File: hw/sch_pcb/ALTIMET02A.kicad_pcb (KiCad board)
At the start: 2 copper layers, 40.1 x 19.8 mm, 14 parts, among them IC1 MS561101BA03-50, J2 HEADER_2x03, J3 HEADER_2x05_PARALLEL

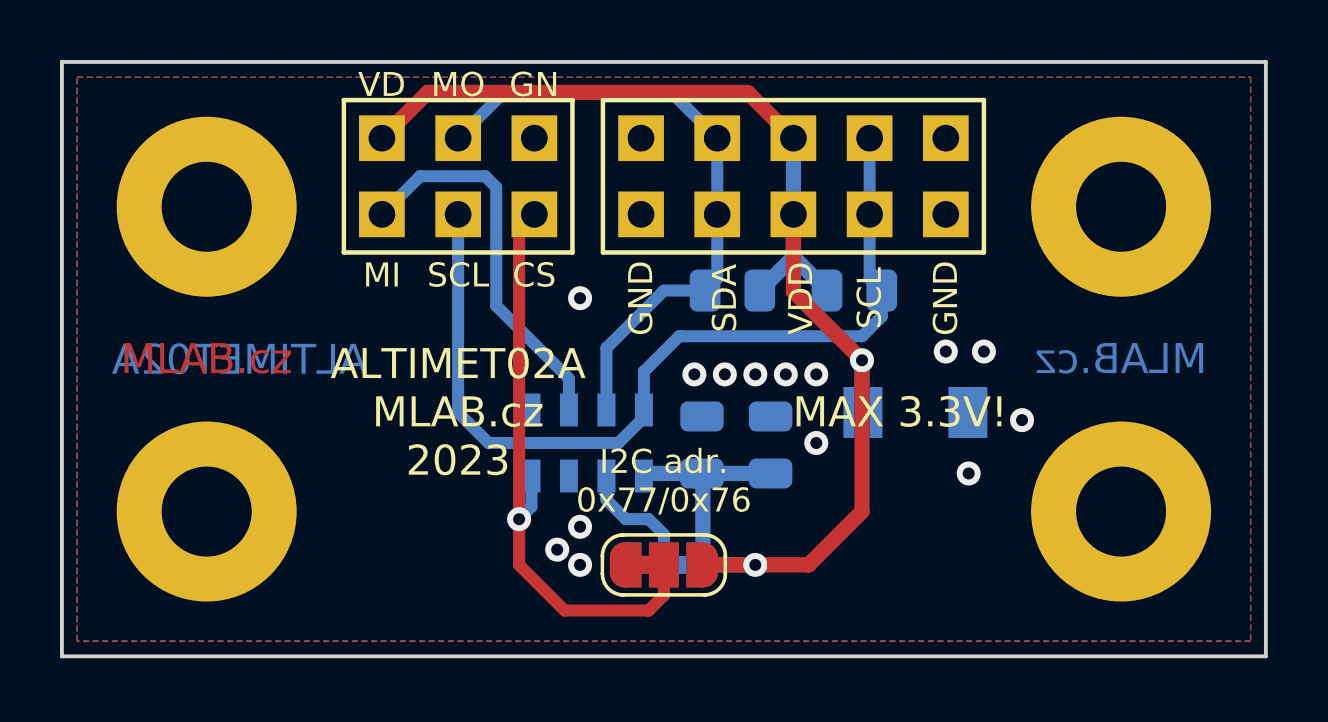
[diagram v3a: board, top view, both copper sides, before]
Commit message: Update submodule Fix CLK in silkscreen.
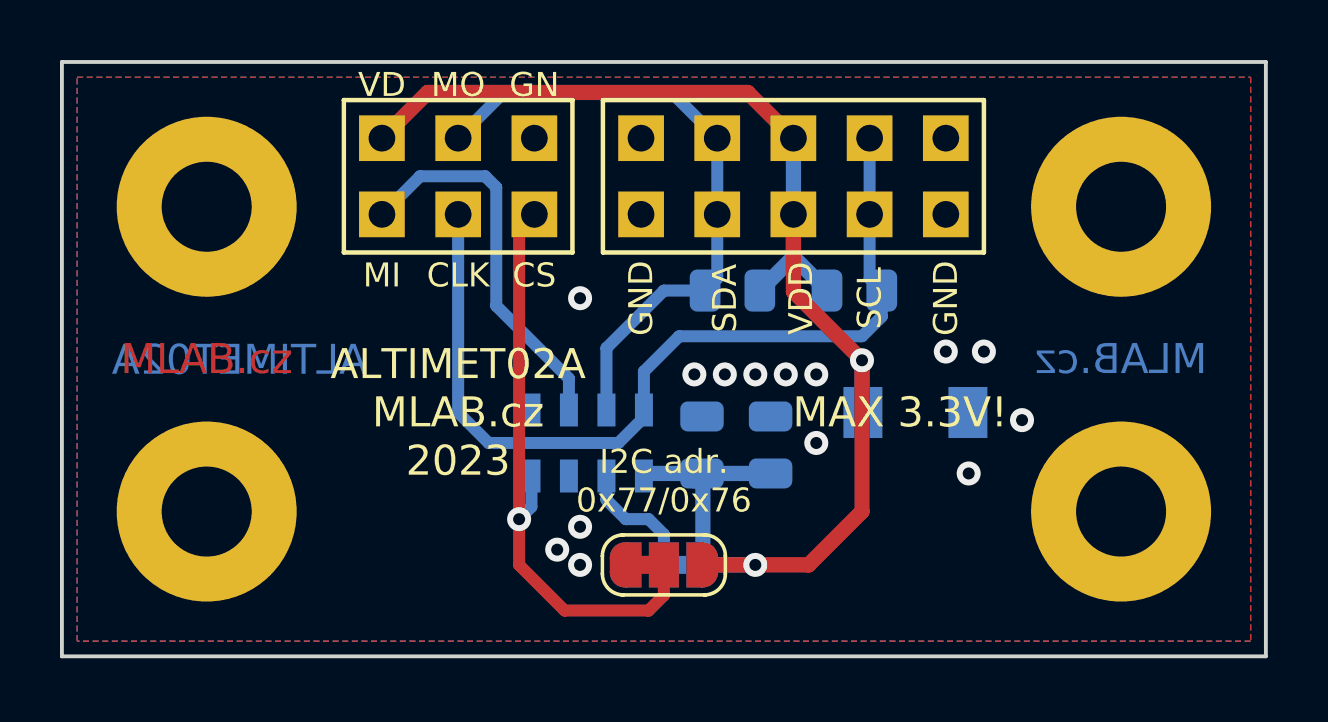
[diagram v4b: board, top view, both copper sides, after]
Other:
- board text added: "CLK"
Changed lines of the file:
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@@
     (effects (font (size 0.8 0.8) (thickness 0.15)))
   )
-  (gr_text "SCL" (at 125.222 103.886) (layer "F.SilkS")
+  (gr_text "CLK" (at 125.222 103.886) (layer "F.SilkS")
     (effects (font (size 0.8 0.8) (thickness 0.15)))
   )
@@
     (pts (xy 152.146 116.586) (xy 152.146 96.774))
     (height 8.89)
-    (gr_text "780 mils" (at 159.886 106.68 90) (layer "Cmts.User")
+    (gr_text "19,812 mm" (at 159.886 106.68 90) (layer "Cmts.User")
       (effects (font (size 1 1) (thickness 0.15)))
     )
@@
     (pts (xy 116.84 101.6) (xy 147.32 101.6))
     (height -7.874)
-    (gr_text "1200 mils" (at 132.08 92.576) (layer "Cmts.User")
+    (gr_text "30,48 mm" (at 132.08 92.576) (layer "Cmts.User")
       (effects (font (size 1 1) (thickness 0.15)))
     )
@@
     (pts (xy 147.32 111.76) (xy 147.32 101.6))
     (height 9.398)
-    (gr_text "400 mils" (at 155.568 106.68 90) (layer "Cmts.User")
+    (gr_text "10,16 mm" (at 155.568 106.68 90) (layer "Cmts.User")
       (effects (font (size 1 1) (thickness 0.15)))
     )
@@
     (pts (xy 112.014 96.774) (xy 152.146 96.774))
     (height -6.858)
-    (gr_text "1580 mils" (at 132.08 88.766) (layer "Cmts.User")
+    (gr_text "40,132 mm" (at 132.08 88.766) (layer "Cmts.User")
       (effects (font (size 1 1) (thickness 0.15)))
     )
